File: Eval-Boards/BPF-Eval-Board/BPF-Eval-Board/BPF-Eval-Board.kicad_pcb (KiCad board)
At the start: 2 copper layers, 61 x 33 mm, 3 parts

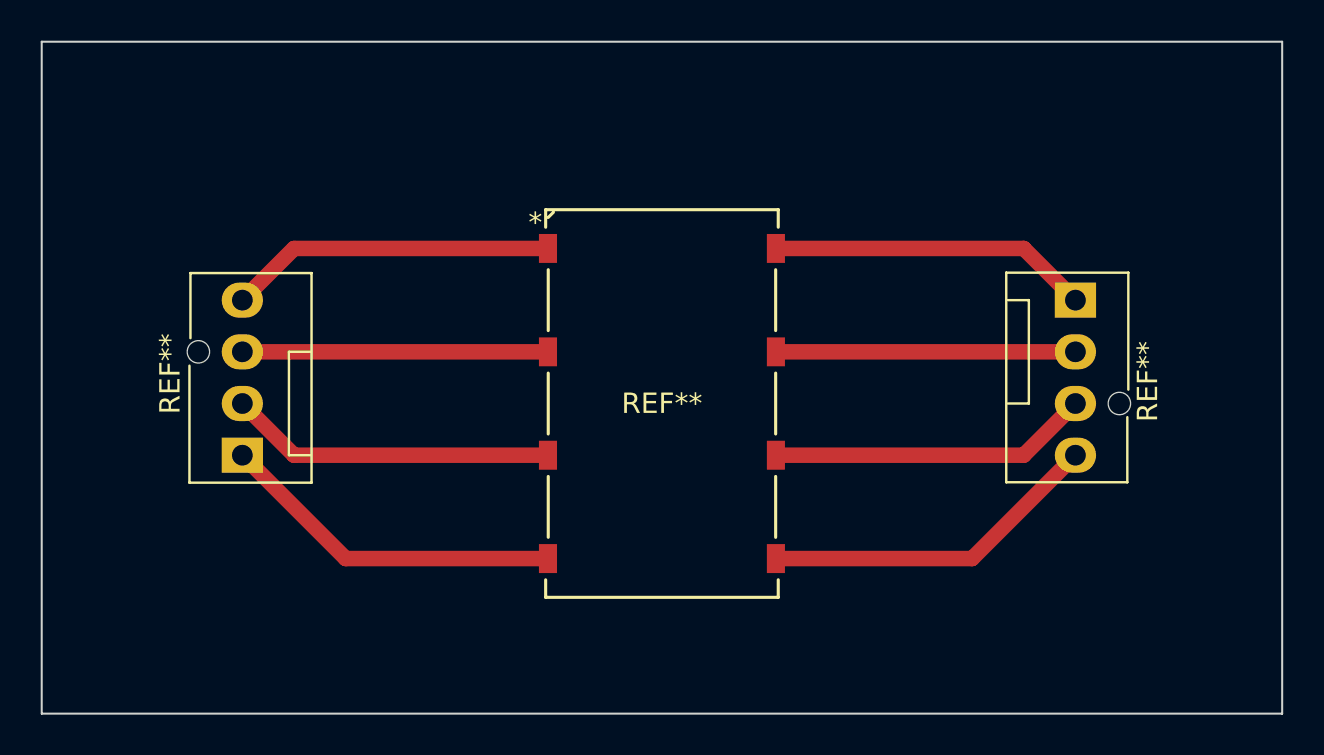
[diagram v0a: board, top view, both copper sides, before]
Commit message: Update BP Eval
Added SMA to BP eval board
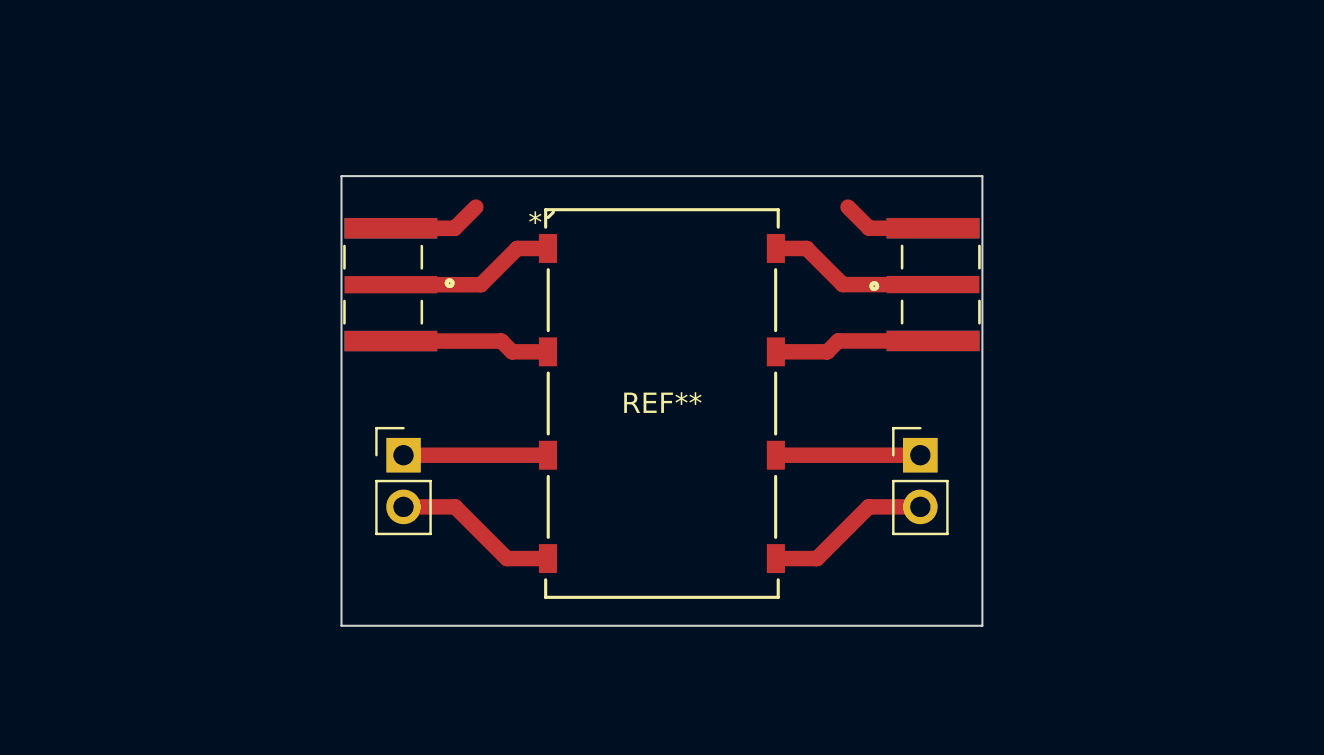
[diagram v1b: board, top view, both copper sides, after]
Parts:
- removed the REF** at (170.2, 88.9)
- removed the REF** at (129.2, 96.5)
- added REF**: PinHeader_1x02_P2.54mm_Vertical, Connector_PinHeader_2.54mm:PinHeader_1x02_P2.54mm_Vertical, F.Cu at (137.2, 96.5)
- added REF**: PinHeader_1x02_P2.54mm_Vertical, Connector_PinHeader_2.54mm:PinHeader_1x02_P2.54mm_Vertical, F.Cu at (162.6, 96.5)
- added REF**: TAOGLAS_EMPCB.SMAFSTJ.B.HT, SMA connectors:TAOGLAS_EMPCB.SMAFSTJ.B.HT, F.Cu at (163.2, 88.1)
- added REF**: TAOGLAS_EMPCB.SMAFSTJ.B.HT, SMA connectors:TAOGLAS_EMPCB.SMAFSTJ.B.HT, F.Cu at (136.5, 88.1)
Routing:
- net (no net): track 127.4 -> 72.5 mm
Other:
- board size 61 x 33 mm -> 31.5 x 22.1 mm

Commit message: new bpf pcb
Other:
- board size 31.5 x 22.1 mm -> 31.5 x 24.6 mm
- board text added: "Macrophthalmus"
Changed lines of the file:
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@@
     (fp_arc (start 5.588 7.874) (mid 5.334 7.62) (end 5.588 7.366)
       (stroke (width 0.0254) (type solid)) (layer "F.Fab"))
-    (pad "1" smd rect (at -5.6007 -7.62) (size 0.889 1.4224) (layers "F.Cu" "F.Paste" "F.Mask"))
-    (pad "2" smd rect (at 5.6007 -7.62) (size 0.889 1.4224) (layers "F.Cu" "F.Paste" "F.Mask"))
-    (pad "3" smd rect (at -5.6007 -2.54) (size 0.889 1.4224) (layers "F.Cu" "F.Paste" "F.Mask"))
-    (pad "4" smd rect (at 5.6007 -2.54) (size 0.889 1.4224) (layers "F.Cu" "F.Paste" "F.Mask"))
-    (pad "5" smd rect (at -5.6007 2.54) (size 0.889 1.4224) (layers "F.Cu" "F.Paste" "F.Mask"))
-    (pad "6" smd rect (at 5.6007 2.54) (size 0.889 1.4224) (layers "F.Cu" "F.Paste" "F.Mask"))
-    (pad "7" smd rect (at -5.6007 7.62) (size 0.889 1.4224) (layers "F.Cu" "F.Paste" "F.Mask"))
-    (pad "8" smd rect (at 5.6007 7.62) (size 0.889 1.4224) (layers "F.Cu" "F.Paste" "F.Mask"))
+    (pad "1" smd rect (at -4.6007 -7.62) (size 1.889 1.4224) (layers "F.Cu" "F.Paste" "F.Mask"))
+    (pad "2" smd rect (at 4.6007 -7.62) (size 1.889 1.4224) (layers "F.Cu" "F.Paste" "F.Mask"))
+    (pad "3" smd rect (at -4.6007 -2.54) (size 1.889 1.4224) (layers "F.Cu" "F.Paste" "F.Mask"))
+    (pad "4" smd rect (at 4.6007 -2.54) (size 1.889 1.4224) (layers "F.Cu" "F.Paste" "F.Mask"))
+    (pad "5" smd rect (at -4.6007 2.54) (size 1.889 1.4224) (layers "F.Cu" "F.Paste" "F.Mask"))
+    (pad "6" smd rect (at 4.6007 2.54) (size 1.889 1.4224) (layers "F.Cu" "F.Paste" "F.Mask"))
+    (pad "7" smd rect (at -4.6007 7.62) (size 1.889 1.4224) (layers "F.Cu" "F.Paste" "F.Mask"))
+    (pad "8" smd rect (at 4.6007 7.62) (size 1.889 1.4224) (layers "F.Cu" "F.Paste" "F.Mask"))
   )
-  (gr_rect (start 134.112 82.804) (end 165.608 104.902)
+  (gr_rect (start 134.112 82.804) (end 165.608 107.442)
     (stroke (width 0.1) (type default)) (fill none) (layer "Edge.Cuts"))
+  (gr_text "Macrophthalmus" (at 134.62 106.68) (layer "F.Cu")
+    (effects (font (size 1.5 1.5) (thickness 0.3) bold) (justify left bottom))
+  )
   (segment (start 158.52275 90.90525) (end 163.1815 90.90525) (width 0.762) (layer "F.Cu") (net 0))
   (segment (start 163.1815 85.36525) (end 160.04125 85.36525) (width 0.762) (layer "F.Cu") (net 0))
